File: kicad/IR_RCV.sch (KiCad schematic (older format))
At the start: 15 parts, among them J1 Host, J2 Slave, Q1 DMN3065LW-7, U4 TLV316IDCKR

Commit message: 回路を改良
受光部をフォトトランジスタに変更
測距センサをVL6180Xに変更
動作電圧を3Vに変更
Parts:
- removed C10: 22p, Capacitors_SMD:C_0201, symbol C
- removed C11: 0.1u, Capacitors_SMD:C_0201, symbol C_Small
- removed C9: 0.01u, Capacitors_SMD:C_0201, symbol C
- removed D3: VEMD2020X01, mouse:VISHAY_DIODE, symbol D_Photo
- removed R7, R8: 1k, Resistors_SMD:R_0201, symbol R
- removed R9: 220k, Resistors_SMD:R_0201, symbol R
- removed U4: TLV316IDCKR, TO_SOT_Packages_SMD:SOT-353_SC-70-5, symbol OPA333DCK
- added Q2: SFH3015FA, mouse:SFH3015FA, symbol Q_Photo_NPN
- C8: value 1u -> 0.22u
- D3: renamed from D2; value VSMB294008G -> SFH4045N; footprint mouse:VISHAY_DIODE -> mouse:SFH4045N
- R7: renamed from R6; value 100k -> 10k
- renumbered R5 to R6
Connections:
- wire segments 44 -> 25
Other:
- note added: "Photo Reflector\nKERI's Lab"
- note removed: "Photo Reflector"
- moved on the sheet: C17, D6, J8, J9, Q8, R13, R14

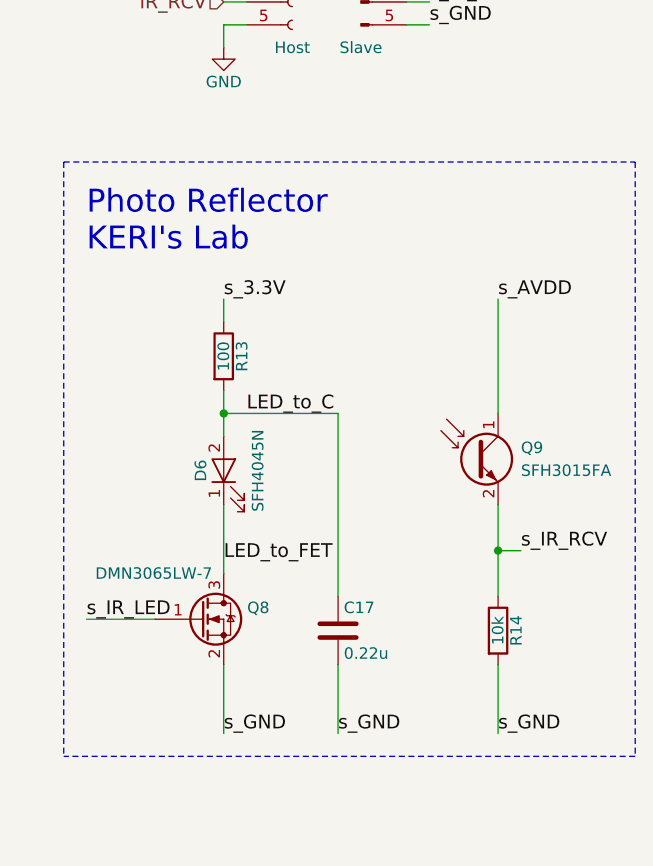
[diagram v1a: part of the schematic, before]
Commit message: 部品を配置
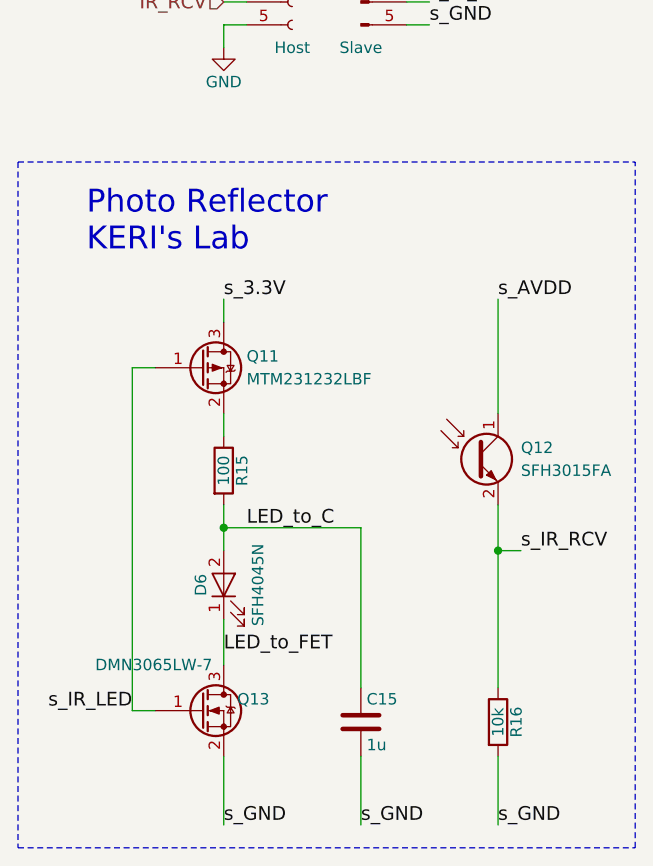
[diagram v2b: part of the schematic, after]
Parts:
- added Q1: MTM231232LBF, TO_SOT_Packages_SMD:SOT-323_SC-70, symbol Q_PMOS_GSD
- C6: renamed from C8; value 0.22u -> 1u; footprint Capacitors_SMD:C_0402 -> Capacitors_SMD:C_0402_NoSilk
- R7: footprint Resistors_SMD:R_0201 -> Resistors_SMD:R_0201_NoSilk
- renumbered Q1 to Q3
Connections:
- net s_3.3V: now also Q1.3 (D); no longer R6.1
- net s_IR_LED: now also Q1.1 (G)
- new net: Q1.2 (S), R6.1
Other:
- moved on the sheet: C15, D6, Q13, R15, R16
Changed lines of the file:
@@
 $Descr A4 11693 8268
 encoding utf-8
-Sheet 4 15
+Sheet 13 16
 Title ""
 Date ""
@@
 Photo Reflector\nKERI's Lab
 $Comp
-L Q_NMOS_GSD Q1
+L Q_NMOS_GSD Q3
 U 1 1 589BE75A
-P 4300 5100
-AR Path="/57CF0B09/589BE75A" Ref="Q1"  Part="1"
-AR Path="/57CF2A30/589BE75A" Ref="Q3"  Part="1"
-AR Path="/597E1B35/589BE75A" Ref="Q6"  Part="1"
-AR Path="/597E1B39/589BE75A" Ref="Q8"  Part="1"
-F 0 "Q8" H 4600 5150 50  0000 R CNN
-F 1 "DMN3065LW-7" H 4350 5300 50  0000 R CNN
-F 2 "TO_SOT_Packages_SMD:SOT-323_SC-70" H 4500 5200 50  0001 C CNN
-F 3 "" H 4300 5100 50  0000 C CNN
-	1    4300 5100
+P 4300 5500
+AR Path="/57CF0B09/589BE75A" Ref="Q3"  Part="1"
+AR Path="/57CF2A30/589BE75A" Ref="Q6"  Part="1"
+AR Path="/597E1B35/589BE75A" Ref="Q10"  Part="1"
+AR Path="/597E1B39/589BE75A" Ref="Q13"  Part="1"
+F 0 "Q13" H 4600 5550 50  0000 R CNN
+F 1 "DMN3065LW-7" H 4350 5700 50  0000 R CNN
+F 2 "TO_SOT_Packages_SMD:SOT-323_SC-70" H 4500 5600 50  0001 C CNN
+F 3 "" H 4300 5500 50  0000 C CNN
+	1    4300 5500
 	1    0    0    -1
 $EndComp
@@
 L R R6
 U 1 1 589BE76D
-P 4400 3950
+P 4400 4450
 AR Path="/57CF0B09/589BE76D" Ref="R6"  Part="1"
 AR Path="/57CF2A30/589BE76D" Ref="R8"  Part="1"
-AR Path="/597E1B35/589BE76D" Ref="R11"  Part="1"
-AR Path="/597E1B39/589BE76D" Ref="R13"  Part="1"
-F 0 "R13" V 4480 3950 50  0000 C CNN
-F 1 "100" V 4400 3950 50  0000 C CNN
-F 2 "Resistors_SMD:R_0603" V 4330 3950 50  0001 C CNN
-F 3 "" H 4400 3950 50  0000 C CNN
-	1    4400 3950
-	1    0    0    -1
-$EndComp
-Text Label 4400 4850 0    60   ~ 0
+AR Path="/597E1B35/589BE76D" Ref="R13"  Part="1"
+AR Path="/597E1B39/589BE76D" Ref="R15"  Part="1"
+F 0 "R15" V 4480 4450 50  0000 C CNN
+F 1 "100" V 4400 4450 50  0000 C CNN
+F 2 "Resistors_SMD:R_0603" V 4330 4450 50  0001 C CNN
+F 3 "" H 4400 4450 50  0000 C CNN
+	1    4400 4450
+	1    0    0    -1
+$EndComp
+Text Label 4400 5250 0    60   ~ 0
 LED_to_FET
-Text Label 4400 5600 0    60   ~ 0
-s_GND
-Text Label 3800 5100 0    60   ~ 0
+Text Label 4400 6000 0    60   ~ 0
+s_GND
+Text Label 4000 5500 2    60   ~ 0
 s_IR_LED
 Text Label 5300 2300 0    60   ~ 0
@@
 Text Label 5300 2100 0    60   ~ 0
 s_3.3V
-Text Label 5600 5600 0    60   ~ 0
+Text Label 5600 6000 0    60   ~ 0
 s_GND
 Text HLabel 4400 2300 0    60   Input ~ 0
 IR_LED
 $Comp
-L GND #PWR038
+L GND #PWR036
 U 1 1 589BF265
 P 4400 2600
-AR Path="/57CF0B09/589BF265" Ref="#PWR038"  Part="1"
-AR Path="/57CF2A30/589BF265" Ref="#PWR041"  Part="1"
-AR Path="/597E1B35/589BF265" Ref="#PWR065"  Part="1"
-AR Path="/597E1B39/589BF265" Ref="#PWR068"  Part="1"
-F 0 "#PWR068" H 4400 2350 50  0001 C CNN
+AR Path="/57CF0B09/589BF265" Ref="#PWR036"  Part="1"
+AR Path="/57CF2A30/589BF265" Ref="#PWR039"  Part="1"
+AR Path="/597E1B35/589BF265" Ref="#PWR063"  Part="1"
+AR Path="/597E1B39/589BF265" Ref="#PWR066"  Part="1"
+F 0 "#PWR066" H 4400 2350 50  0001 C CNN
 F 1 "GND" H 4400 2450 50  0000 C CNN
 F 2 "" H 4400 2600 50  0000 C CNN
@@
 Text Label 4400 3700 0    60   ~ 0
 s_3.3V
-Text Label 4900 5600 0    60   ~ 0
-s_GND
-Text Label 4500 4200 0    60   ~ 0
+Text Label 5000 6000 0    60   ~ 0
+s_GND
+Text Label 4500 4700 0    60   ~ 0
 LED_to_C
 Wire Wire Line
@@
 Wire Wire Line
 	4500 2300 4400 2300
-Connection ~ 4400 4200
-Wire Wire Line
-	4900 4200 4400 4200
-Wire Wire Line
-	4900 5000 4900 4200
-Wire Wire Line
-	4900 5600 4900 5300
+Connection ~ 4400 4700
+Wire Wire Line
+	4400 4700 5000 4700
+Wire Wire Line
+	5000 6000 5000 5700
 Wire Wire Line
 	4100 2000 4100 2200
 Wire Wire Line
-	4400 4300 4400 4100
-Wire Wire Line
-	4400 4600 4400 4900
-Wire Notes Line
-	3700 3100 3700 5700
-Wire Wire Line
-	5600 5300 5600 5600
+	4400 4800 4400 4600
+Wire Wire Line
+	5600 5700 5600 6000
 Wire Wire Line
 	5300 2400 5200 2400
@@
 	5200 2100 5300 2100
 Wire Wire Line
-	4400 3800 4400 3700
-Wire Wire Line
-	4400 5300 4400 5600
-Wire Wire Line
-	3800 5100 4100 5100
+	4400 4300 4400 4200
+Wire Wire Line
+	4400 5700 4400 6000
 Text Label 5600 3700 0    60   ~ 0
 s_AVDD
@@
 L LED D3
 U 1 1 594AC674
-P 4400 4450
+P 4400 4950
 AR Path="/57CF0B09/594AC674" Ref="D3"  Part="1"
 AR Path="/57CF2A30/594AC674" Ref="D4"  Part="1"
 AR Path="/597E1B35/594AC674" Ref="D5"  Part="1"
 AR Path="/597E1B39/594AC674" Ref="D6"  Part="1"
-F 0 "D6" H 4400 4550 50  0000 C CNN
-F 1 "SFH4045N" H 4400 4300 50  0000 C CNN
-F 2 "mouse:SFH4045N" H 4400 4450 50  0001 C CNN
-F 3 "" H 4400 4450 50  0001 C CNN
-	1    4400 4450
+F 0 "D6" H 4400 5050 50  0000 C CNN
+F 1 "SFH4045N" H 4400 4800 50  0000 C CNN
+F 2 "mouse:SFH4045N" H 4400 4950 50  0001 C CNN
+F 3 "" H 4400 4950 50  0001 C CNN
+	1    4400 4950
 	0    -1   -1   0
 $EndComp
 $Comp
-L VDDA #PWR039
+L VDDA #PWR037
 U 1 1 59C54857
 P 4100 2000
-AR Path="/57CF0B09/59C54857" Ref="#PWR039"  Part="1"
-AR Path="/57CF2A30/59C54857" Ref="#PWR042"  Part="1"
-AR Path="/597E1B35/59C54857" Ref="#PWR066"  Part="1"
-AR Path="/597E1B39/59C54857" Ref="#PWR069"  Part="1"
-F 0 "#PWR069" H 4100 1850 50  0001 C CNN
+AR Path="/57CF0B09/59C54857" Ref="#PWR037"  Part="1"
+AR Path="/57CF2A30/59C54857" Ref="#PWR040"  Part="1"
+AR Path="/597E1B35/59C54857" Ref="#PWR064"  Part="1"
+AR Path="/597E1B39/59C54857" Ref="#PWR067"  Part="1"
+F 0 "#PWR067" H 4100 1850 50  0001 C CNN
 F 1 "VDDA" H 4100 2150 50  0000 C CNN
 F 2 "" H 4100 2000 50  0001 C CNN
@@
 $EndComp
 $Comp
-L +3.3V #PWR040
+L +3.3V #PWR038
 U 1 1 5A172FEF
 P 4400 2000
-AR Path="/57CF0B09/5A172FEF" Ref="#PWR040"  Part="1"
-AR Path="/57CF2A30/5A172FEF" Ref="#PWR043"  Part="1"
-AR Path="/597E1B35/5A172FEF" Ref="#PWR067"  Part="1"
-AR Path="/597E1B39/5A172FEF" Ref="#PWR070"  Part="1"
-F 0 "#PWR070" H 4400 1850 50  0001 C CNN
+AR Path="/57CF0B09/5A172FEF" Ref="#PWR038"  Part="1"
+AR Path="/57CF2A30/5A172FEF" Ref="#PWR041"  Part="1"
+AR Path="/597E1B35/5A172FEF" Ref="#PWR065"  Part="1"
+AR Path="/597E1B39/5A172FEF" Ref="#PWR068"  Part="1"
+F 0 "#PWR068" H 4400 1850 50  0001 C CNN
 F 1 "+3.3V" H 4400 2140 50  0000 C CNN
 F 2 "" H 4400 2000 50  0001 C CNN
@@
 s_AVDD
 $Comp
-L C C8
+L C C6
 U 1 1 5A1B992B
-P 4900 5150
-AR Path="/57CF0B09/5A1B992B" Ref="C8"  Part="1"
-AR Path="/57CF2A30/5A1B992B" Ref="C9"  Part="1"
-AR Path="/597E1B35/5A1B992B" Ref="C16"  Part="1"
-AR Path="/597E1B39/5A1B992B" Ref="C17"  Part="1"
-F 0 "C17" H 4925 5250 50  0000 L CNN
-F 1 "0.22u" H 4925 5050 50  0000 L CNN
-F 2 "Capacitors_SMD:C_0402" H 4938 5000 50  0001 C CNN
-F 3 "" H 4900 5150 50  0001 C CNN
-	1    4900 5150
+P 5000 5550
+AR Path="/57CF0B09/5A1B992B" Ref="C6"  Part="1"
+AR Path="/57CF2A30/5A1B992B" Ref="C7"  Part="1"
+AR Path="/597E1B35/5A1B992B" Ref="C14"  Part="1"
+AR Path="/597E1B39/5A1B992B" Ref="C15"  Part="1"
+F 0 "C15" H 5025 5650 50  0000 L CNN
+F 1 "1u" H 5025 5450 50  0000 L CNN
+F 2 "Capacitors_SMD:C_0402_NoSilk" H 5038 5400 50  0001 C CNN
+F 3 "" H 5000 5550 50  0001 C CNN
+	1    5000 5550
 	1    0    0    -1
 $EndComp
@@
 P 5500 4400
 AR Path="/57CF0B09/5A4ADF8B" Ref="Q2"  Part="1"
-AR Path="/57CF2A30/5A4ADF8B" Ref="Q4"  Part="1"
-AR Path="/597E1B35/5A4ADF8B" Ref="Q7"  Part="1"
-AR Path="/597E1B39/5A4ADF8B" Ref="Q9"  Part="1"
-F 0 "Q9" H 5700 4450 50  0000 L CNN
+AR Path="/57CF2A30/5A4ADF8B" Ref="Q5"  Part="1"
+AR Path="/597E1B35/5A4ADF8B" Ref="Q9"  Part="1"
+AR Path="/597E1B39/5A4ADF8B" Ref="Q12"  Part="1"
+F 0 "Q12" H 5700 4450 50  0000 L CNN
 F 1 "SFH3015FA" H 5700 4350 50  0000 L CNN
 F 2 "mouse:SFH3015FA" H 5700 4500 50  0001 C CNN
@@
 L R R7
 U 1 1 589BEE3B
-P 5600 5150
+P 5600 5550
 AR Path="/57CF0B09/589BEE3B" Ref="R7"  Part="1"
 AR Path="/57CF2A30/589BEE3B" Ref="R9"  Part="1"
-AR Path="/597E1B35/589BEE3B" Ref="R12"  Part="1"
-AR Path="/597E1B39/589BEE3B" Ref="R14"  Part="1"
-F 0 "R14" V 5680 5150 50  0000 C CNN
-F 1 "10k" V 5600 5150 50  0000 C CNN
-F 2 "Resistors_SMD:R_0201" V 5530 5150 50  0001 C CNN
-F 3 "" H 5600 5150 50  0000 C CNN
-	1    5600 5150
+AR Path="/597E1B35/589BEE3B" Ref="R14"  Part="1"
+AR Path="/597E1B39/589BEE3B" Ref="R16"  Part="1"
+F 0 "R16" V 5680 5550 50  0000 C CNN
+F 1 "10k" V 5600 5550 50  0000 C CNN
+F 2 "Resistors_SMD:R_0201_NoSilk" V 5530 5550 50  0001 C CNN
+F 3 "" H 5600 5550 50  0000 C CNN
+	1    5600 5550
 	1    0    0    -1
 $EndComp
@@
 	5700 4800 5600 4800
 Connection ~ 5600 4800
-Wire Wire Line
-	5600 4600 5600 5000
-Wire Notes Line
-	3700 3100 6200 3100
-Wire Notes Line
-	6200 3100 6200 5700
-Wire Notes Line
-	6200 5700 3700 5700
+Wire Notes Line
+	3500 3100 6200 3100
+Wire Notes Line
+	3500 6100 6200 6100
+$Comp
+L Q_PMOS_GSD Q1
+U 1 1 5AB4DD07
+P 4300 4000
+AR Path="/57CF0B09/5AB4DD07" Ref="Q1"  Part="1"
+AR Path="/57CF2A30/5AB4DD07" Ref="Q4"  Part="1"
+AR Path="/597E1B35/5AB4DD07" Ref="Q8"  Part="1"
+AR Path="/597E1B39/5AB4DD07" Ref="Q11"  Part="1"
+F 0 "Q11" H 4500 4050 50  0000 L CNN
+F 1 "MTM231232LBF" H 4500 3950 50  0000 L CNN
+F 2 "TO_SOT_Packages_SMD:SOT-323_SC-70" H 4500 4100 50  0001 C CNN
+F 3 "" H 4300 4000 50  0001 C CNN
+	1    4300 4000
+	1    0    0    -1
+$EndComp
+Wire Wire Line
+	4400 3700 4400 3800
+Wire Wire Line
+	4100 5500 4000 5500
+Wire Wire Line
+	4100 4000 4000 4000
+Wire Wire Line
+	4400 5300 4400 5100
+Wire Wire Line
+	5000 4700 5000 5400
+Wire Wire Line
+	4000 4000 4000 5500
+Wire Wire Line
+	5600 5400 5600 4600
+Wire Notes Line
+	6200 6100 6200 3100
+Wire Notes Line
+	3500 3100 3500 6100
 $EndSCHEMATC

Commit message: 回路図を改良
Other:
- note added: "Photo Reflector v20180503\nKERI's Lab"
- note removed: "Photo Reflector\nKERI's Lab"
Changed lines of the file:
@@
 $Descr A4 11693 8268
 encoding utf-8
-Sheet 13 16
+Sheet 5 16
 Title ""
 Date ""
@@
 Text HLabel 4400 2400 0    60   Input ~ 0
 IR_RCV
-Text Notes 3800 3500 0    100  ~ 0
-Photo Reflector\nKERI's Lab
+Text Notes 3500 3600 0    79   ~ 0
+Photo Reflector v20180503\nKERI's Lab
 $Comp
 L Q_NMOS_GSD Q3
@@
 AR Path="/597E1B35/589BE75A" Ref="Q10"  Part="1"
 AR Path="/597E1B39/589BE75A" Ref="Q13"  Part="1"
-F 0 "Q13" H 4600 5550 50  0000 R CNN
-F 1 "DMN3065LW-7" H 4350 5700 50  0000 R CNN
+F 0 "Q6" H 4300 5650 50  0000 R CNN
+F 1 "DMN3065LW-7" H 4350 5350 50  0000 R CNN
 F 2 "TO_SOT_Packages_SMD:SOT-323_SC-70" H 4500 5600 50  0001 C CNN
 F 3 "" H 4300 5500 50  0000 C CNN
@@
 AR Path="/597E1B35/589BE76D" Ref="R13"  Part="1"
 AR Path="/597E1B39/589BE76D" Ref="R15"  Part="1"
-F 0 "R15" V 4480 4450 50  0000 C CNN
+F 0 "R8" V 4480 4450 50  0000 C CNN
 F 1 "100" V 4400 4450 50  0000 C CNN
 F 2 "Resistors_SMD:R_0603" V 4330 4450 50  0001 C CNN
@@
 Text Label 4400 6000 0    60   ~ 0
 s_GND
-Text Label 4000 5500 2    60   ~ 0
+Text Label 3900 5500 2    60   ~ 0
 s_IR_LED
 Text Label 5300 2300 0    60   ~ 0
@@
 AR Path="/597E1B35/589BF265" Ref="#PWR063"  Part="1"
 AR Path="/597E1B39/589BF265" Ref="#PWR066"  Part="1"
-F 0 "#PWR066" H 4400 2350 50  0001 C CNN
+F 0 "#PWR039" H 4400 2350 50  0001 C CNN
 F 1 "GND" H 4400 2450 50  0000 C CNN
 F 2 "" H 4400 2600 50  0000 C CNN
@@
 AR Path="/597E1B35/594AC674" Ref="D5"  Part="1"
 AR Path="/597E1B39/594AC674" Ref="D6"  Part="1"
-F 0 "D6" H 4400 5050 50  0000 C CNN
-F 1 "SFH4045N" H 4400 4800 50  0000 C CNN
+F 0 "D4" V 4500 4800 50  0000 C CNN
+F 1 "SFH4045N" V 4400 4650 50  0000 C CNN
 F 2 "mouse:SFH4045N" H 4400 4950 50  0001 C CNN
 F 3 "" H 4400 4950 50  0001 C CNN
@@
 AR Path="/597E1B35/59C54857" Ref="#PWR064"  Part="1"
 AR Path="/597E1B39/59C54857" Ref="#PWR067"  Part="1"
-F 0 "#PWR067" H 4100 1850 50  0001 C CNN
+F 0 "#PWR040" H 4100 1850 50  0001 C CNN
 F 1 "VDDA" H 4100 2150 50  0000 C CNN
 F 2 "" H 4100 2000 50  0001 C CNN
@@
 AR Path="/597E1B35/5A172E6D" Ref="J6"  Part="1"
 AR Path="/597E1B39/5A172E6D" Ref="J8"  Part="1"
-F 0 "J8" H 4700 2600 50  0000 C CNN
+F 0 "J3" H 4700 2600 50  0000 C CNN
 F 1 "Host" H 4700 2000 50  0000 C CNN
 F 2 "mouse:STAND_HOST_05" H 4700 2300 50  0001 C CNN
@@
 AR Path="/597E1B35/5A172FEF" Ref="#PWR065"  Part="1"
 AR Path="/597E1B39/5A172FEF" Ref="#PWR068"  Part="1"
-F 0 "#PWR068" H 4400 1850 50  0001 C CNN
+F 0 "#PWR041" H 4400 1850 50  0001 C CNN
 F 1 "+3.3V" H 4400 2140 50  0000 C CNN
 F 2 "" H 4400 2000 50  0001 C CNN
@@
 AR Path="/597E1B35/5A17311F" Ref="J7"  Part="1"
 AR Path="/597E1B39/5A17311F" Ref="J9"  Part="1"
-F 0 "J9" H 5000 2600 50  0000 C CNN
+F 0 "J4" H 5000 2600 50  0000 C CNN
 F 1 "Slave" H 5000 2000 50  0000 C CNN
 F 2 "mouse:STAND_SLAVE_05" H 5000 2300 50  0001 C CNN
@@
 AR Path="/597E1B35/5A1B992B" Ref="C14"  Part="1"
 AR Path="/597E1B39/5A1B992B" Ref="C15"  Part="1"
-F 0 "C15" H 5025 5650 50  0000 L CNN
+F 0 "C7" H 5025 5650 50  0000 L CNN
 F 1 "1u" H 5025 5450 50  0000 L CNN
 F 2 "Capacitors_SMD:C_0402_NoSilk" H 5038 5400 50  0001 C CNN
@@
 AR Path="/597E1B35/5A4ADF8B" Ref="Q9"  Part="1"
 AR Path="/597E1B39/5A4ADF8B" Ref="Q12"  Part="1"
-F 0 "Q12" H 5700 4450 50  0000 L CNN
+F 0 "Q5" H 5700 4450 50  0000 L CNN
 F 1 "SFH3015FA" H 5700 4350 50  0000 L CNN
 F 2 "mouse:SFH3015FA" H 5700 4500 50  0001 C CNN
@@
 AR Path="/597E1B35/589BEE3B" Ref="R14"  Part="1"
 AR Path="/597E1B39/589BEE3B" Ref="R16"  Part="1"
-F 0 "R16" V 5680 5550 50  0000 C CNN
+F 0 "R9" V 5680 5550 50  0000 C CNN
 F 1 "10k" V 5600 5550 50  0000 C CNN
 F 2 "Resistors_SMD:R_0201_NoSilk" V 5530 5550 50  0001 C CNN
@@
 Connection ~ 5600 4800
 Wire Notes Line
-	3500 3100 6200 3100
-Wire Notes Line
-	3500 6100 6200 6100
+	3400 6100 6200 6100
 $Comp
 L Q_PMOS_GSD Q1
@@
 AR Path="/597E1B35/5AB4DD07" Ref="Q8"  Part="1"
 AR Path="/597E1B39/5AB4DD07" Ref="Q11"  Part="1"
-F 0 "Q11" H 4500 4050 50  0000 L CNN
+F 0 "Q4" H 4500 4050 50  0000 L CNN
 F 1 "MTM231232LBF" H 4500 3950 50  0000 L CNN
 F 2 "TO_SOT_Packages_SMD:SOT-323_SC-70" H 4500 4100 50  0001 C CNN
@@
 	4400 3700 4400 3800
 Wire Wire Line
-	4100 5500 4000 5500
+	3900 5500 4100 5500
 Wire Wire Line
 	4100 4000 4000 4000
@@
 Wire Wire Line
 	5600 5400 5600 4600
-Wire Notes Line
-	6200 6100 6200 3100
-Wire Notes Line
-	3500 3100 3500 6100
+Connection ~ 4000 5500
+Wire Notes Line
+	3400 3300 3400 6100
+Wire Notes Line
+	3400 3300 6200 3300
+Wire Notes Line
+	6200 3300 6200 6100
 $EndSCHEMATC

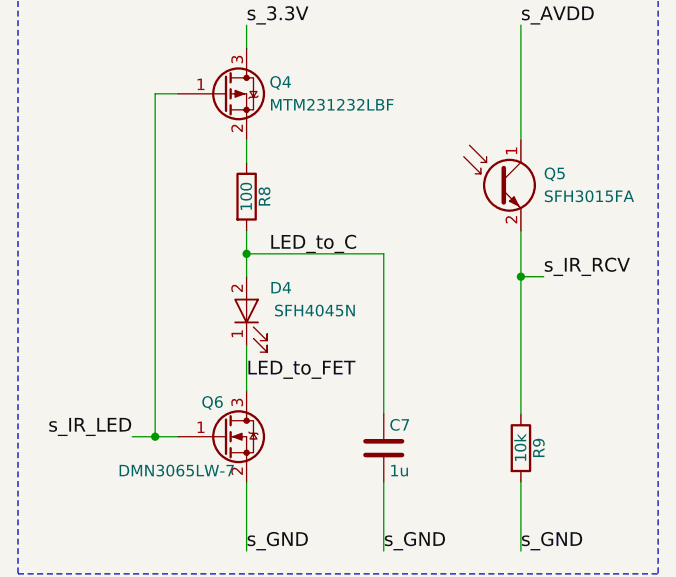
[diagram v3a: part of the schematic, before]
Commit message: 回路を編集 ToFを除去
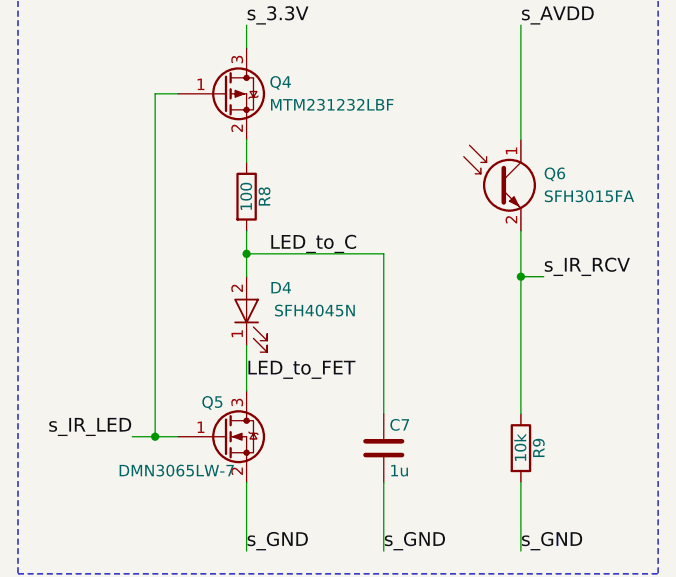
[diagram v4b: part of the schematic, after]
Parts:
- renumbered Q3 to Q2, Q2 to Q3
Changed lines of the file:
@@
 $Descr A4 11693 8268
 encoding utf-8
-Sheet 5 16
+Sheet 13 15
 Title ""
 Date ""
@@
 Photo Reflector v20180503\nKERI's Lab
 $Comp
-L Q_NMOS_GSD Q3
+L Q_NMOS_GSD Q2
 U 1 1 589BE75A
 P 4300 5500
-AR Path="/57CF0B09/589BE75A" Ref="Q3"  Part="1"
-AR Path="/57CF2A30/589BE75A" Ref="Q6"  Part="1"
-AR Path="/597E1B35/589BE75A" Ref="Q10"  Part="1"
-AR Path="/597E1B39/589BE75A" Ref="Q13"  Part="1"
-F 0 "Q6" H 4300 5650 50  0000 R CNN
+AR Path="/57CF0B09/589BE75A" Ref="Q2"  Part="1"
+AR Path="/57CF2A30/589BE75A" Ref="Q5"  Part="1"
+AR Path="/597E1B35/589BE75A" Ref="Q9"  Part="1"
+AR Path="/597E1B39/589BE75A" Ref="Q12"  Part="1"
+F 0 "Q5" H 4300 5650 50  0000 R CNN
 F 1 "DMN3065LW-7" H 4350 5350 50  0000 R CNN
 F 2 "TO_SOT_Packages_SMD:SOT-323_SC-70" H 4500 5600 50  0001 C CNN
@@
 AR Path="/597E1B35/589BF265" Ref="#PWR063"  Part="1"
 AR Path="/597E1B39/589BF265" Ref="#PWR066"  Part="1"
-F 0 "#PWR039" H 4400 2350 50  0001 C CNN
+F 0 "#PWR066" H 4400 2350 50  0001 C CNN
 F 1 "GND" H 4400 2450 50  0000 C CNN
 F 2 "" H 4400 2600 50  0000 C CNN
@@
 AR Path="/597E1B35/59C54857" Ref="#PWR064"  Part="1"
 AR Path="/597E1B39/59C54857" Ref="#PWR067"  Part="1"
-F 0 "#PWR040" H 4100 1850 50  0001 C CNN
+F 0 "#PWR067" H 4100 1850 50  0001 C CNN
 F 1 "VDDA" H 4100 2150 50  0000 C CNN
 F 2 "" H 4100 2000 50  0001 C CNN
@@
 AR Path="/597E1B35/5A172FEF" Ref="#PWR065"  Part="1"
 AR Path="/597E1B39/5A172FEF" Ref="#PWR068"  Part="1"
-F 0 "#PWR041" H 4400 1850 50  0001 C CNN
+F 0 "#PWR068" H 4400 1850 50  0001 C CNN
 F 1 "+3.3V" H 4400 2140 50  0000 C CNN
 F 2 "" H 4400 2000 50  0001 C CNN
@@
 $EndComp
 $Comp
-L Q_Photo_NPN Q2
+L Q_Photo_NPN Q3
 U 1 1 5A4ADF8B
 P 5500 4400
-AR Path="/57CF0B09/5A4ADF8B" Ref="Q2"  Part="1"
-AR Path="/57CF2A30/5A4ADF8B" Ref="Q5"  Part="1"
-AR Path="/597E1B35/5A4ADF8B" Ref="Q9"  Part="1"
-AR Path="/597E1B39/5A4ADF8B" Ref="Q12"  Part="1"
-F 0 "Q5" H 5700 4450 50  0000 L CNN
+AR Path="/57CF0B09/5A4ADF8B" Ref="Q3"  Part="1"
+AR Path="/57CF2A30/5A4ADF8B" Ref="Q6"  Part="1"
+AR Path="/597E1B35/5A4ADF8B" Ref="Q10"  Part="1"
+AR Path="/597E1B39/5A4ADF8B" Ref="Q13"  Part="1"
+F 0 "Q6" H 5700 4450 50  0000 L CNN
 F 1 "SFH3015FA" H 5700 4350 50  0000 L CNN
 F 2 "mouse:SFH3015FA" H 5700 4500 50  0001 C CNN
